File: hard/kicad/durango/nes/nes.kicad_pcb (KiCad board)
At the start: 2 copper layers, 6 parts, among them J1 NES 0, J2 NES 1, J3 IOx, U1 74HC139, U2 74HC125, U3 74HC08

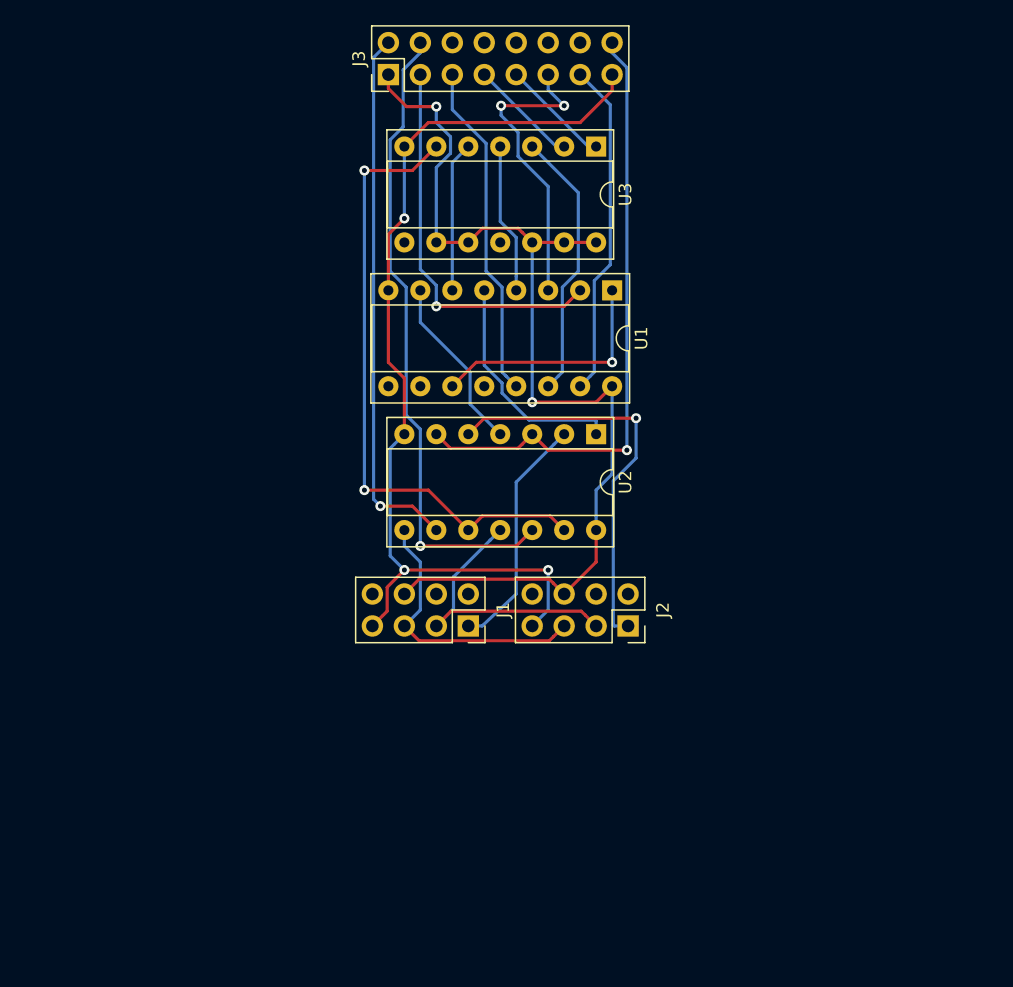
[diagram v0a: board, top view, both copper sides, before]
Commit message: complete revamp of NES interface
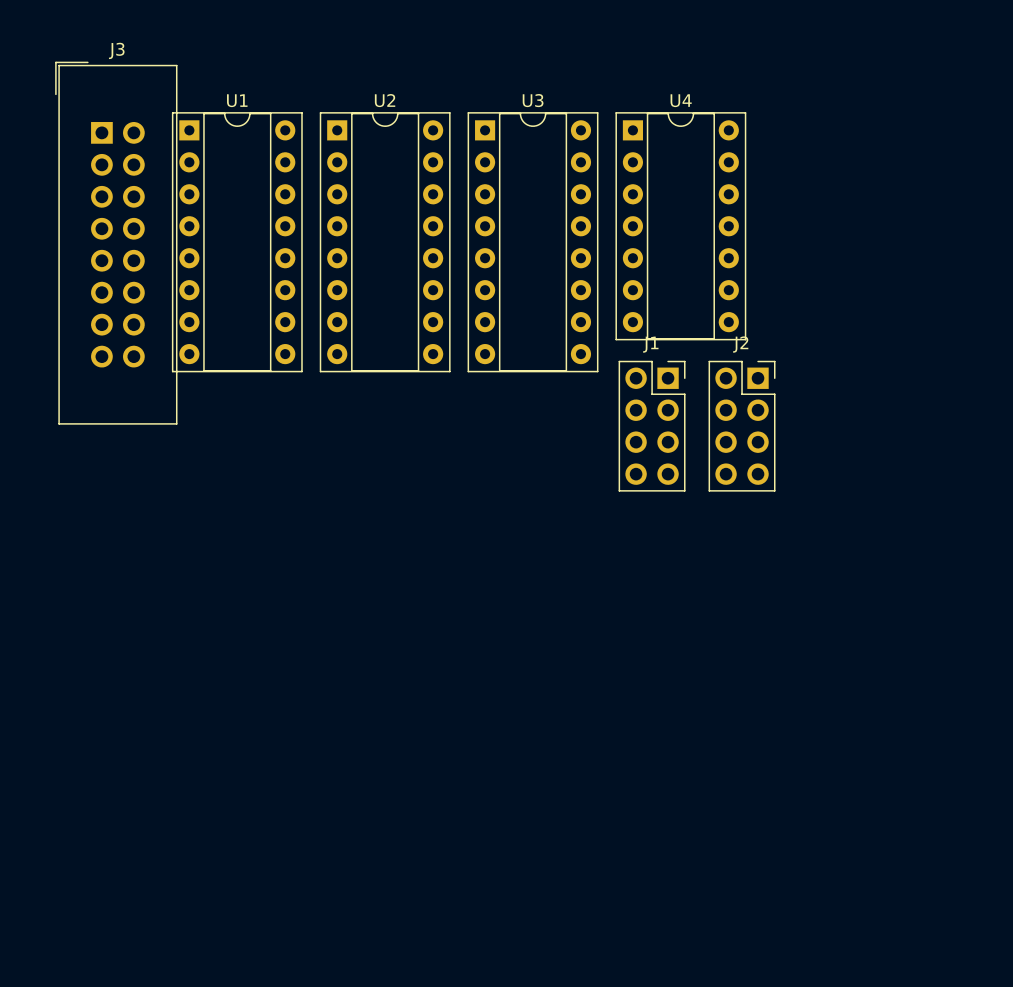
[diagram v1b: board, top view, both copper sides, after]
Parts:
- added U4: 74HC04, Package_DIP:DIP-14_W7.62mm_Socket, F.Cu at (72.8, 21.6)
- J3: footprint Connector_PinHeader_2.54mm:PinHeader_2x08_P2.54mm_Vertical -> Connector_IDC:IDC-Header_2x08_P2.54mm_Vertical
- U1: value 74HC139 -> 74HC595
- U2: value 74HC125 -> 74HC595; footprint Package_DIP:DIP-14_W7.62mm_Socket -> Package_DIP:DIP-16_W7.62mm_Socket
- U3: value 74HC08 -> 74HC138; footprint Package_DIP:DIP-14_W7.62mm_Socket -> Package_DIP:DIP-16_W7.62mm_Socket
- moved U1 35.9 mm to (37.5, 21.6), turned to 0 degrees
- moved U2 31.7 mm to (49.3, 21.6), turned to 0 degrees
- moved J1 25.3 mm to (75.6, 41.3), turned to 0 degrees
- moved J3 23.2 mm to (30.6, 21.8), turned to 0 degrees
- moved J2 22.2 mm to (82.7, 41.3), turned to 0 degrees
- moved U3 8.92 mm to (61.0, 21.6), turned to 0 degrees
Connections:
- J1 pad 1: /NES0D -> /NESD0
- J1 pad 3: /NES0L -> /NESLAT
- J1 pad 5: /NES0C -> /NESCLK
- J2 pad 1: /NES1D -> /NESD1
- J2 pad 3: /NES0L -> /NESLAT
- J2 pad 5: /NES0C -> /NESCLK
- J3 pad 10: (no net) -> /PD4
- J3 pad 11: /R~W -> /BR~W
- J3 pad 12: (no net) -> /PD5
- J3 pad 13: /~IO9 -> /~IOX
- J3 pad 14: (no net) -> /PD6
- J3 pad 3: /PA0 -> /BA0
- J3 pad 5: /PA1 -> /BA1
- J3 pad 6: (no net) -> /PD2
- J3 pad 7: /PA2 -> /BA2
- J3 pad 8: (no net) -> /PD3
- J3 pad 9: /PA3 -> /BA3
- U1 pad 1: /~NES -> /PD1
- U1 pad 10: (no net) -> +5V
- U1 pad 11: /~NES -> /NESCLK
- U1 pad 12: (no net) -> /~RCLK
- U1 pad 13: /PA1 -> /~RD0
- U1 pad 14: /HSEL -> /NESD0
- U1 pad 15: /~IO9 -> /PD0
- U1 pad 2: /PA0 -> /PD2
- U1 pad 3: /R~W -> /PD3
- U1 pad 4: /CL0 -> /PD4
- U1 pad 5: /DAT0 -> /PD5
- U1 pad 6: /CL1 -> /PD6
- U1 pad 7: /DAT1 -> /PD7
- U2 pad 1: /DAT0 -> /PD1
- U2 pad 10: /CLK-STB -> +5V
- U2 pad 11: /NES0L -> /NESCLK
- U2 pad 12: /PD1 -> /~RCLK
- U2 pad 13: /CLK-STB -> /~RD1
- U2 pad 14: +5V -> /NESD1
- U2 pad 2: /NES0D -> /PD2
- U2 pad 3: /PD7 -> /PD3
- U2 pad 4: /DAT1 -> /PD4
- U2 pad 5: /NES1D -> /PD5
- U2 pad 6: /PD7 -> /PD6
- U2 pad 7: GND -> /PD7
- U2 pad 8: /NES0C -> GND
- U2 pad 9: /PD0 -> (no net)
- U3 pad 1: /PA3 -> /BR~W
- U3 pad 10: +5V -> /~RD0
- U3 pad 11: (no net) -> /~NESLAT
- U3 pad 12: +5V -> (no net)
- U3 pad 13: +5V -> (no net)
- U3 pad 14: +5V -> (no net)
- U3 pad 2: /PA2 -> /BA0
- U3 pad 3: /HSEL -> /BA2
- U3 pad 4: /CL0 -> /BA1
- U3 pad 5: /CL1 -> /~IOX
- U3 pad 6: /CLK-STB -> /BA3
- U3 pad 7: GND -> /~RD1
- U3 pad 8: (no net) -> GND
- U3 pad 9: +5V -> /~NESCLK
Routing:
- net +5V: track 82.2 -> 0.00 mm, vias 2 -> 0
- net GND: track 77.2 -> 0.00 mm, vias 3 -> 0
- net /PD1: track 51.4 -> 0.00 mm, vias 1 -> 0
- net /CLK-STB: track 50.0 -> 0.00 mm, vias 2 -> 0
- net /PD7: track 49.5 -> 0.00 mm, vias 1 -> 0
- net /PD0: track 42.8 -> 0.00 mm, vias 1 -> 0
- net /NES1D: track 32.3 -> 0.00 mm, vias 1 -> 0
- net /PA0: track 30.9 -> 0.00 mm, vias 1 -> 0
- net /PA1: track 26.9 -> 0.00 mm
- net /~IO9: track 26.7 -> 0.00 mm
- net /R~W: track 24.2 -> 0.00 mm, vias 2 -> 0
- net /NES0L: track 23.4 -> 0.00 mm
- net /NES0C: track 22.3 -> 0.00 mm
- net /HSEL: track 21.6 -> 0.00 mm
- net /~NES: track 19.2 -> 0.00 mm, vias 1 -> 0
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
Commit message: preliminary NES interface PCB
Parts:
- moved J3 58.2 mm to (30.5, 80.0), turned to 180 degrees
- moved U3 46.4 mm to (38.7, 62.2)
- moved U1 42.6 mm to (50.2, 62.2)
- moved U2 42.5 mm to (61.6, 62.2)
- moved U4 41.9 mm to (73.0, 63.5)
- moved J2 29.8 mm to (97.2, 67.3)
- moved J1 29.3 mm to (88.9, 67.3)
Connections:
- net /~RCLK renamed /RCLK
- J1 pad 1: /NESD0 -> /N0D
- J2 pad 1: /NESD1 -> /N1D
- U1 pad 14: /NESD0 -> /~NESD0
- U2 pad 14: /NESD1 -> /~NESD1
- U4 pad 10: (no net) -> /~NESD0
- U4 pad 11: +5V -> /N0D
- U4 pad 8: (no net) -> /~NESD1
- U4 pad 9: +5V -> /N1D
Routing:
- net +5V: track 0.00 -> 131.2 mm
- net GND: track 0.00 -> 88.2 mm
- net /PD0: track 0.00 -> 64.7 mm, vias 0 -> 1
- net /PD7: track 0.00 -> 52.4 mm, vias 0 -> 2
- net /PD1: track 0.00 -> 49.4 mm, vias 0 -> 2
- net /PD6: track 0.00 -> 48.1 mm, vias 0 -> 2
- net /PD2: track 0.00 -> 46.0 mm, vias 0 -> 2
- net /NESCLK: track 0.00 -> 45.8 mm
- net /PD5: track 0.00 -> 43.1 mm, vias 0 -> 2
- net /~NESLAT: track 0.00 -> 42.2 mm, vias 0 -> 1
- net /~RD1: track 0.00 -> 40.6 mm
- net /PD3: track 0.00 -> 39.6 mm, vias 0 -> 2
- net /~NESCLK: track 0.00 -> 39.3 mm, vias 0 -> 1
- net /PD4: track 0.00 -> 36.2 mm
- net /NESLAT: track 0.00 -> 34.8 mm, vias 0 -> 1
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- added copper zone on B.Cu, net +5V
- added copper zone on F.Cu, net GND

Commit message: pullups for NES interface
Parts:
- added R1: 220K, Resistor_THT:R_Axial_DIN0204_L3.6mm_D1.6mm_P2.54mm_Vertical, F.Cu at (86.4, 59.7)
- added R2: 220K, Resistor_THT:R_Axial_DIN0204_L3.6mm_D1.6mm_P2.54mm_Vertical, F.Cu at (95.2, 59.7)
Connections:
- U1 pad 1: /PD1 -> /PD2
- U1 pad 2: /PD2 -> /PD1
- U1 pad 4: /PD4 -> /PD6
- U1 pad 5: /PD5 -> /PD4
- U1 pad 6: /PD6 -> /PD5
- U2 pad 1: /PD1 -> /PD2
- U2 pad 2: /PD2 -> /PD1
- U2 pad 4: /PD4 -> /PD6
- U2 pad 5: /PD5 -> /PD4
- U2 pad 6: /PD6 -> /PD5

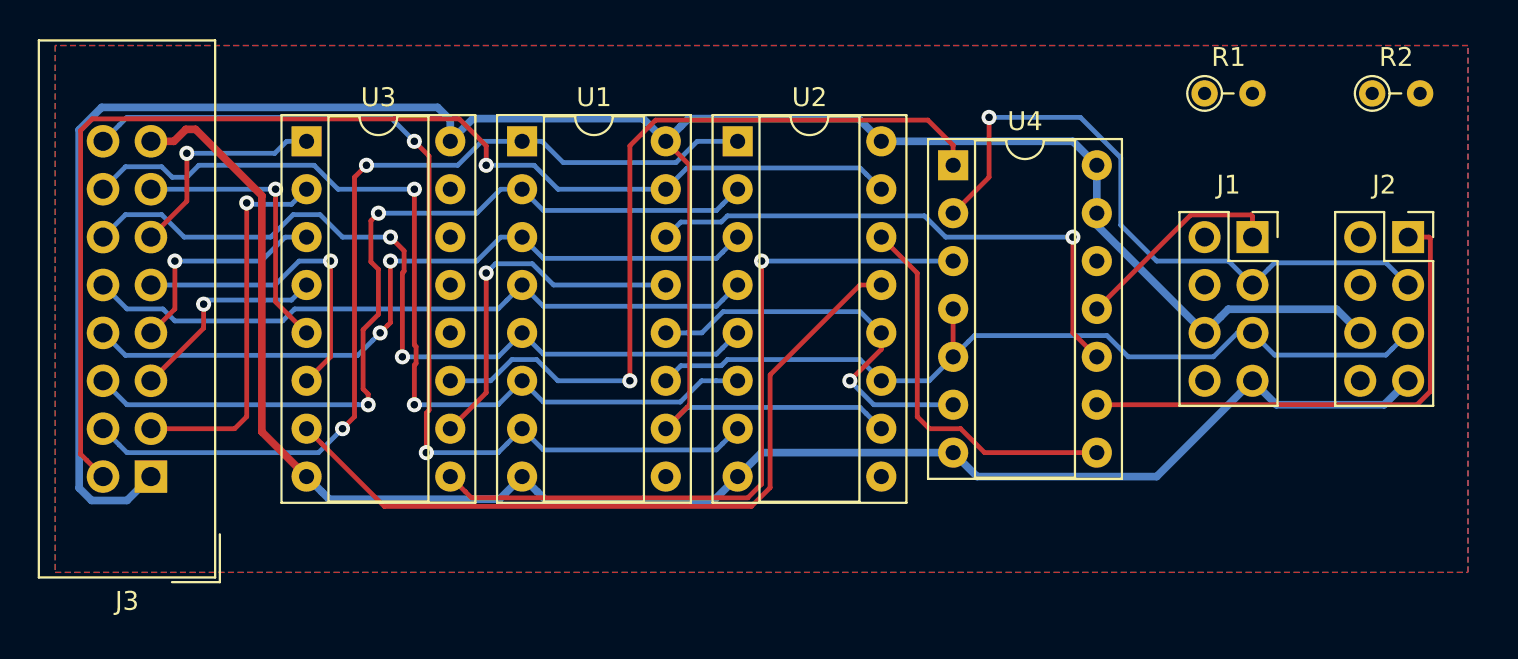
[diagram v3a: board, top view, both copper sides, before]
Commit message: switch NES board connections
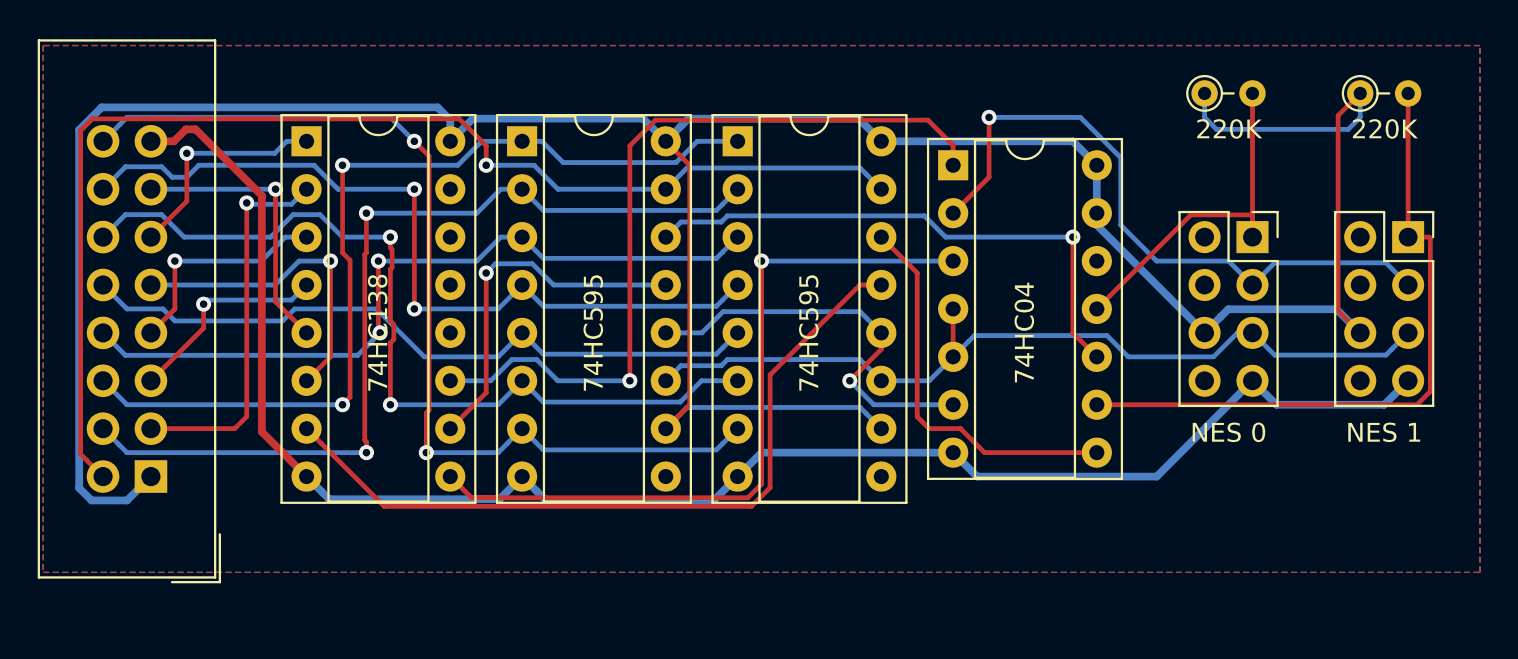
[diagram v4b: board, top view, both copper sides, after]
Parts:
- moved R2 0.64 mm to (94.6, 59.7)
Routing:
- net +5V: track 131.2 -> 156.2 mm
- net /N0D: track 11.5 -> 19.1 mm
- net /N1D: track 27.3 -> 34.9 mm
- net /PD6: track 48.1 -> 43.0 mm
- net /PD5: track 43.1 -> 46.2 mm
- net /PD2: track 46.0 -> 48.7 mm
- net /PD4: track 36.2 -> 37.2 mm
- net /PD1: track 49.4 -> 48.4 mm
